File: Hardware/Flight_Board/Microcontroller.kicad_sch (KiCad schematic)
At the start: 18 parts, among them J1 Conn_01x06, J2 Conn_01x04, SW1 SW_Push, U1 STM32F411RCTx, U2 FT5HN

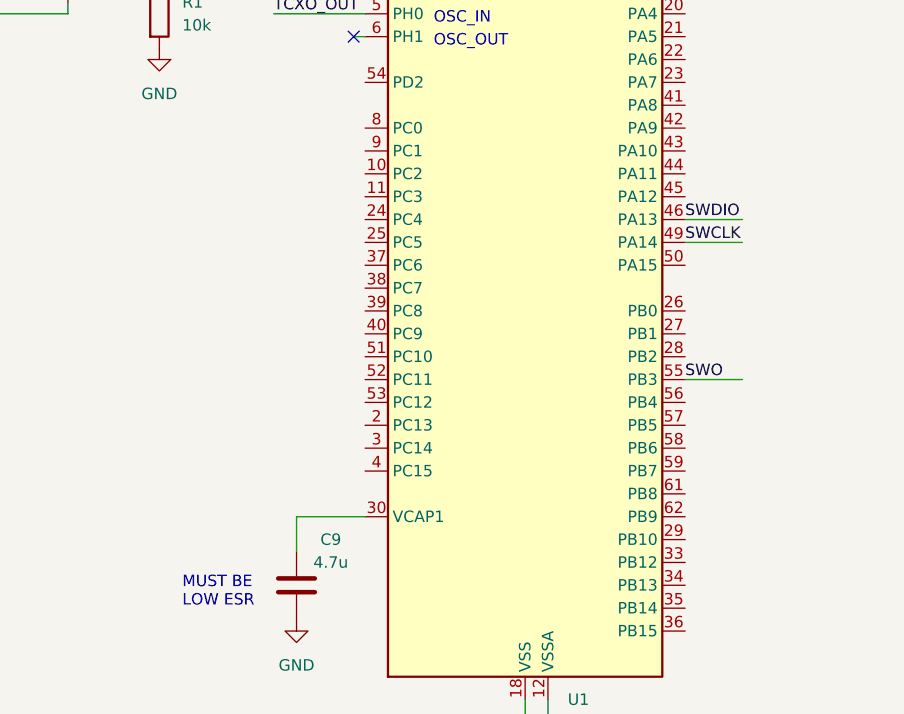
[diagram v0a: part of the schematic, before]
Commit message: standardize connections and create initial spi2 bus
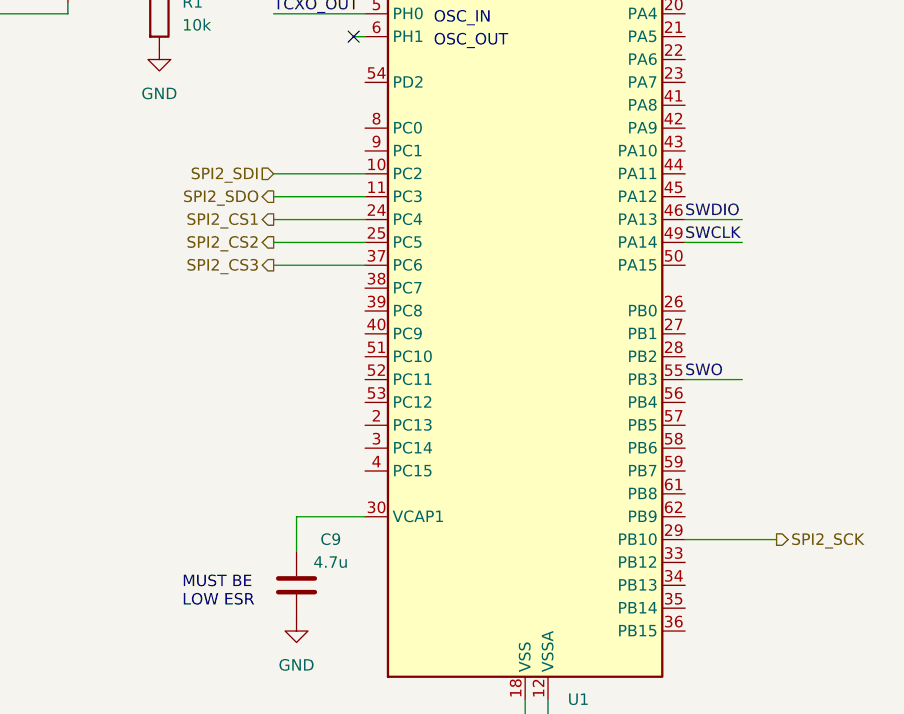
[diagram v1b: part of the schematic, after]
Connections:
- net SPI2_SDI: now reaches U1.10 (PC2)
- net SPI2_SDO: now reaches U1.11 (PC3)
- net SPI2_CS1: now reaches U1.24 (PC4)
- net SPI2_CS2: now reaches U1.25 (PC5)
- net SPI2_SCK: now reaches U1.29 (PB10)
- net SPI2_CS3: now reaches U1.37 (PC6)
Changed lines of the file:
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@@
+    (stroke (width 0) (type default))
+  )
+  (wire (pts (xy 166.37 88.9) (xy 176.53 88.9))
     (stroke (width 0) (type default))
   )
@@
     (stroke (width 0) (type default))
   )
+  (wire (pts (xy 166.37 93.98) (xy 176.53 93.98))
+    (stroke (width 0) (type default))
+  )
   (wire (pts (xy 77.47 25.4) (xy 88.9 25.4))
     (stroke (width 0) (type default))
@@
     (stroke (width 0) (type default))
   )
+  (wire (pts (xy 166.37 96.52) (xy 176.53 96.52))
+    (stroke (width 0) (type default))
+  )
   (wire (pts (xy 196.85 50.8) (xy 196.85 53.34))
     (stroke (width 0) (type default))
@@
     (stroke (width 0) (type default))
   )
+  (wire (pts (xy 212.09 127) (xy 222.25 127))
+    (stroke (width 0) (type default))
+  )
   (wire (pts (xy 26.67 36.83) (xy 26.67 40.64))
     (stroke (width 0) (type default))
@@
     (stroke (width 0) (type default))
   )
+  (wire (pts (xy 166.37 91.44) (xy 176.53 91.44))
+    (stroke (width 0) (type default))
+  )
   (wire (pts (xy 199.39 50.8) (xy 199.39 53.34))
     (stroke (width 0) (type default))
@@
   )
   (wire (pts (xy 130.81 68.58) (xy 143.51 68.58))
+    (stroke (width 0) (type default))
+  )
+  (wire (pts (xy 166.37 86.36) (xy 176.53 86.36))
     (stroke (width 0) (type default))
   )
@@
     (effects (font (size 1.27 1.27)) (justify left bottom))
   )
+  (hierarchical_label "SPI2_CS2" (shape output) (at 166.37 93.98 180) (fields_autoplaced)
+    (effects (font (size 1.27 1.27)) (justify right))
+  )
+  (hierarchical_label "SPI2_SDI" (shape input) (at 166.37 86.36 180) (fields_autoplaced)
+    (effects (font (size 1.27 1.27)) (justify right))
+  )
+  (hierarchical_label "SPI2_SDO" (shape output) (at 166.37 88.9 180) (fields_autoplaced)
+    (effects (font (size 1.27 1.27)) (justify right))
+  )
+  (hierarchical_label "SPI2_CS1" (shape output) (at 166.37 91.44 180) (fields_autoplaced)
+    (effects (font (size 1.27 1.27)) (justify right))
+  )
+  (hierarchical_label "SPI2_CS3" (shape output) (at 166.37 96.52 180) (fields_autoplaced)
+    (effects (font (size 1.27 1.27)) (justify right))
+  )
+  (hierarchical_label "SPI2_SCK" (shape output) (at 222.25 127 0) (fields_autoplaced)
+    (effects (font (size 1.27 1.27)) (justify left))
+  )
   (symbol (lib_id "Device:R") (at 153.67 68.58 0) (unit 1)

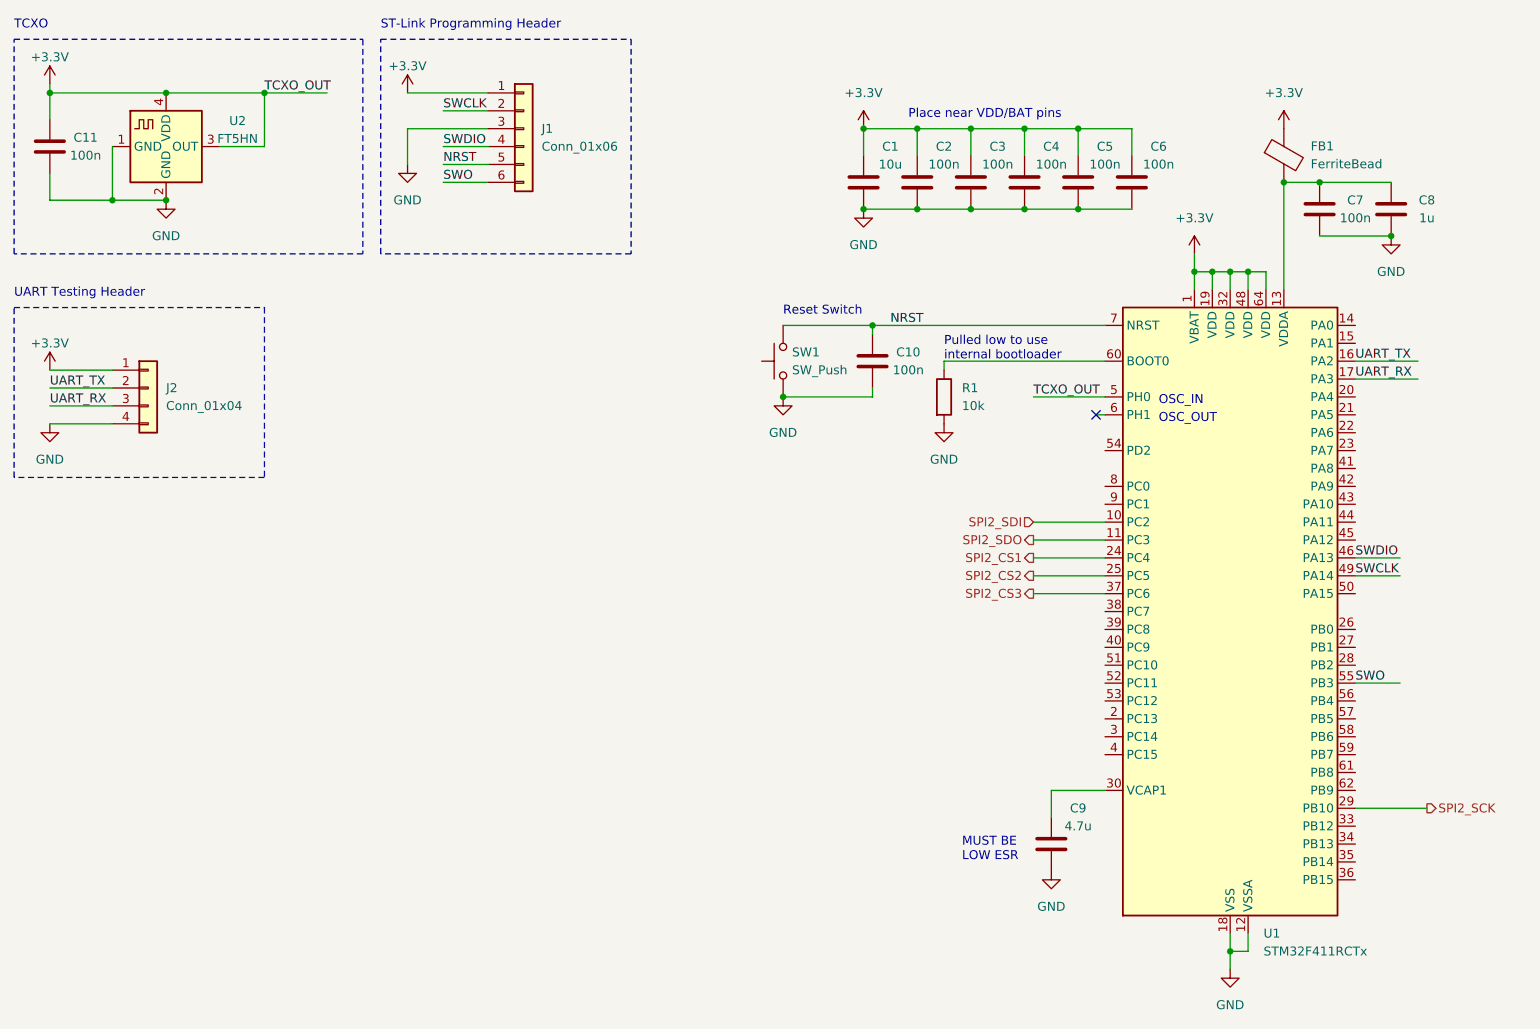
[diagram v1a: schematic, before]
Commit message: move ADLX375 to I2C, bring out more mcu pins, and general touchups
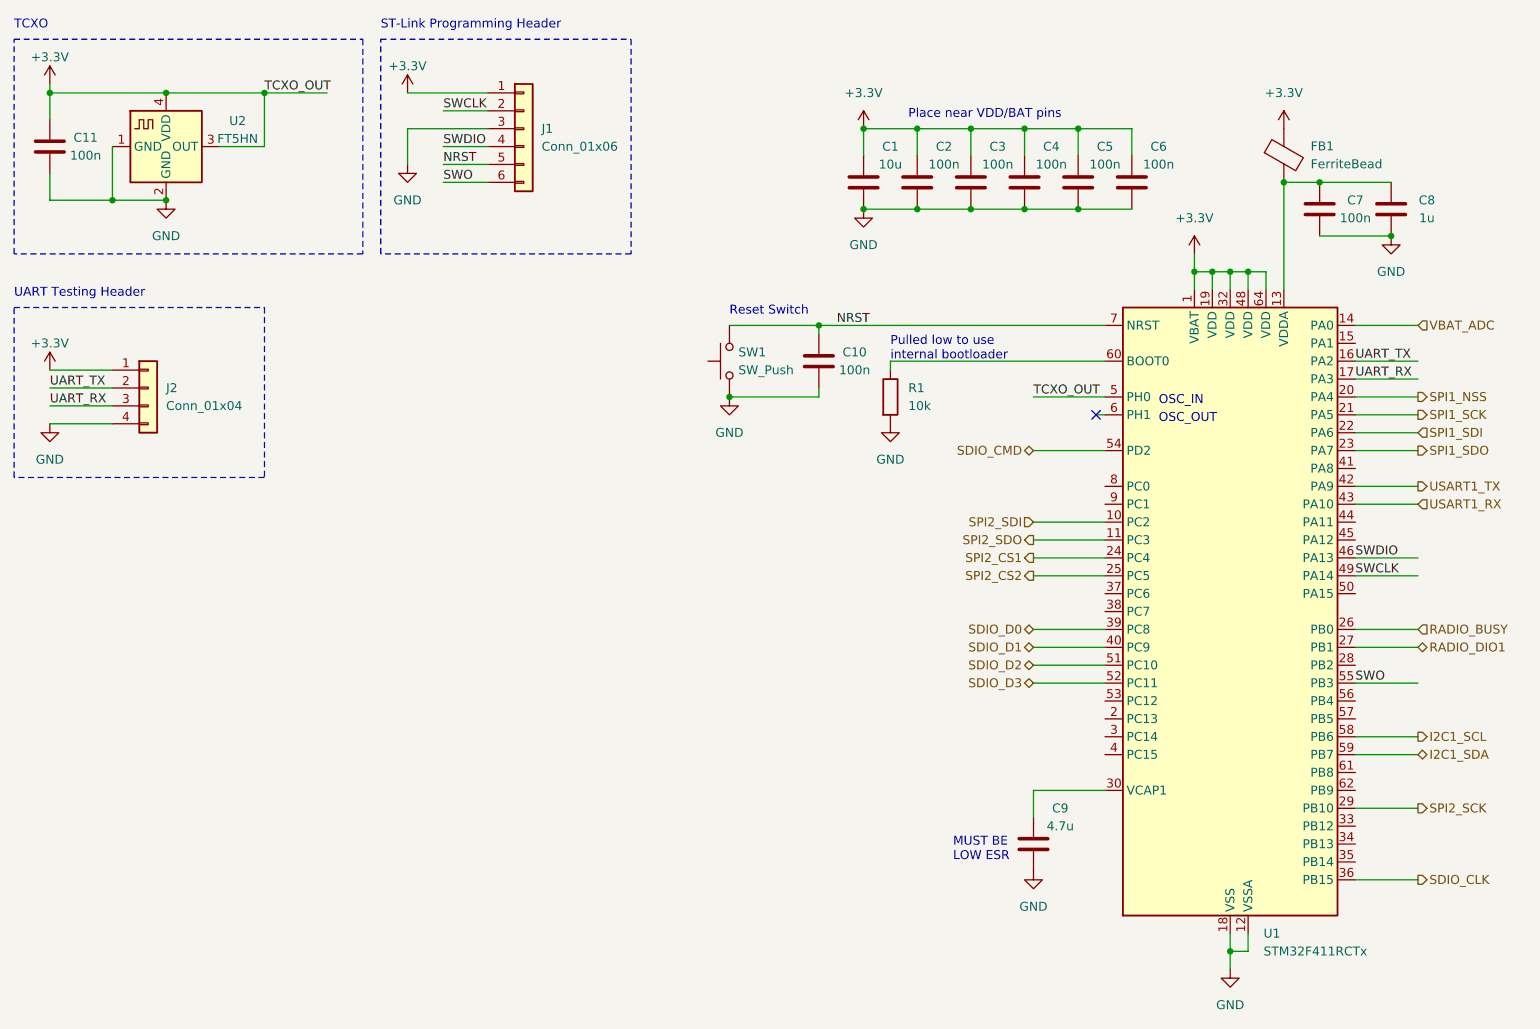
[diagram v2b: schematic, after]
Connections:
- net VBAT_ADC: now reaches U1.14 (PA0)
- net SPI1_NSS: now reaches U1.20 (PA4)
- net SPI1_SCK: now reaches U1.21 (PA5)
- net SPI1_SDI: now reaches U1.22 (PA6)
- net SPI1_SDO: now reaches U1.23 (PA7)
- net RADIO_BUSY: now reaches U1.26 (PB0)
- net RADIO_DIO1: now reaches U1.27 (PB1)
- net SDIO_CLK: now reaches U1.36 (PB15)
- net SDIO_D0: now reaches U1.39 (PC8)
- net SDIO_D1: now reaches U1.40 (PC9)
- net USART1_TX: now reaches U1.42 (PA9)
- net USART1_RX: now reaches U1.43 (PA10)
- net SDIO_D2: now reaches U1.51 (PC10)
- net SDIO_D3: now reaches U1.52 (PC11)
- net SDIO_CMD: now reaches U1.54 (PD2)
- net I2C1_SCL: now reaches U1.58 (PB6)
- net I2C1_SDA: now reaches U1.59 (PB7)
- net SPI2_CS3: no longer names the net of U1.37 (PC6)
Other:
- moved on the sheet: C10, C9, R1, SW1

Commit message: clean up and finalize initial design
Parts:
- added R23: 22k, symbol Device:R
- added R24: 10k, symbol Device:R
- renumbered C11 to C1, C7 to C10, C8 to C11, C10 to C2, C1 to C3, C2 to C4, C3 to C5, C4 to C6, C9 to C7, C5 to C8, C6 to C9, J2 to J3, J1 to J4, U2 to U1, U1 to U?
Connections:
- net GND: now also R24.2
- net VBAT_ADC: now also R23.2, R24.1
- net SW_ST2: now reaches U?.2 (PC13)
- net RADIO_RST: now reaches U?.28 (PB2)
- net SW_ST3: now reaches U?.3 (PC14)
- net SW_EN3: now reaches U?.37 (PC6)
- net SW_EN4: now reaches U?.38 (PC7)
- net SW_ST4: now reaches U?.4 (PC15)
- net SW_ST1: now reaches U?.53 (PC12)
- net SW_EN1: now reaches U?.8 (PC0)
- net SW_EN2: now reaches U?.9 (PC1)
- new net VBAT: R23.1
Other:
- note added: "VBat Voltage Divider"
